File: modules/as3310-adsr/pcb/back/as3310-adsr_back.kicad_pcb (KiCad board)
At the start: 2 copper layers, 18.3 x 94 mm, 23 parts, among them J1 IDC Header 2x8, J2 Pin Socket 1x9, U1 AS3310, U2 TL071

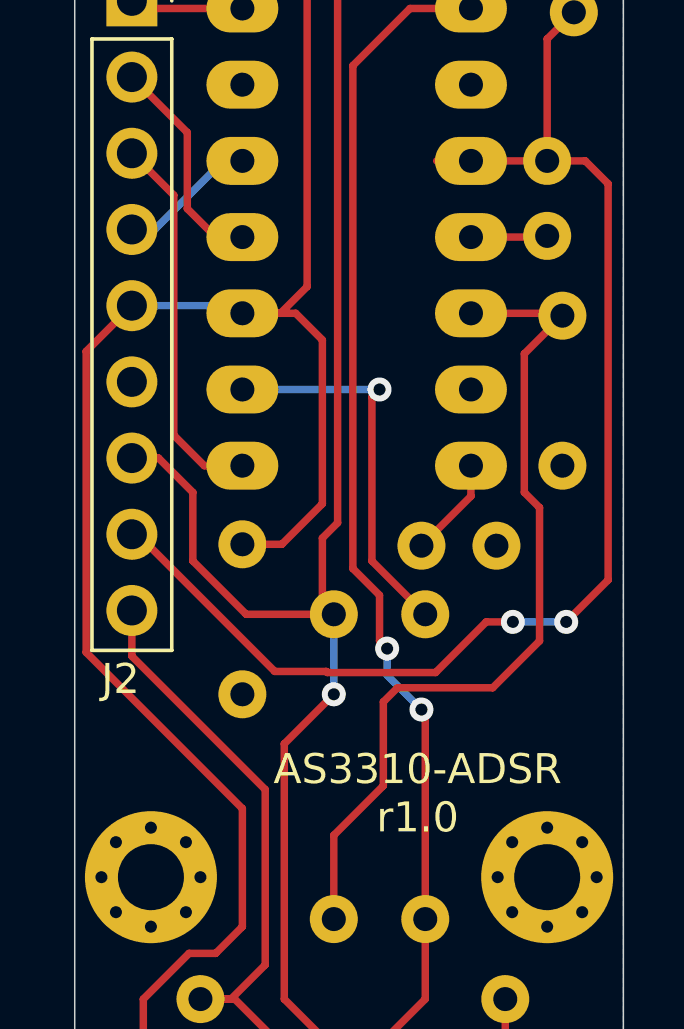
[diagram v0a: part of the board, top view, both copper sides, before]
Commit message: modules: as3310-adsr: new revision for back pcb: 1.1
the module was missing a diode in the gate input to avoid burning the
AS3310 by applying negative voltage.

I fixed my boards by cutting and scrapping the gate track, close to R3
top pin and soldering an SMD version of 1N4148, like this:

https://filebin.xyz/UGnlaM44cwMN2fDaeGj87lC2
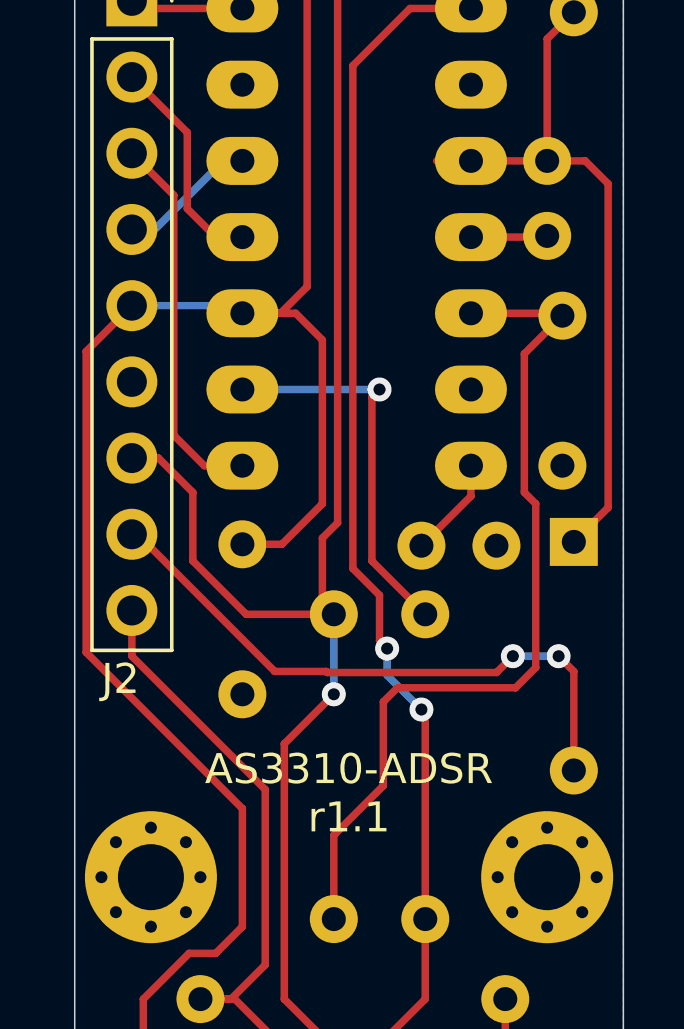
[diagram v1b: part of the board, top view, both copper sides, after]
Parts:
- added D1: 1N4148, Diode_THT:D_DO-35_SOD27_P7.62mm_Horizontal, B.Cu at (163.3, 114.0)
- C2: value 3n -> 3.3n
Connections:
- C2 pad 1: GATE -> Net-(C2-Pad1)
- R1 pad 2: GATE -> Net-(C2-Pad1)
- U1 pad 4: GATE -> Net-(C2-Pad1)
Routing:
- net Net-(C2-Pad1): track 0.00 -> 23.8 mm
- net GATE: track 43.6 -> 20.4 mm
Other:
- board text added: "AS3310-ADSR r1.1"
- board text removed: "AS3310-ADSR r1.0"

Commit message: modules: as3310-adsr: back: upgrade to kicad 6
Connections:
- J1 pad 11: (no net) -> unconnected-(J1-Pad11)
- J1 pad 12: (no net) -> unconnected-(J1-Pad12)
- J1 pad 13: (no net) -> unconnected-(J1-Pad13)
- J1 pad 14: (no net) -> unconnected-(J1-Pad14)
- J1 pad 15: (no net) -> unconnected-(J1-Pad15)
- J1 pad 16: (no net) -> unconnected-(J1-Pad16)
- U1 pad 16: (no net) -> unconnected-(U1-Pad16)
- U1 pad 3: (no net) -> unconnected-(U1-Pad3)
- U2 pad 1: (no net) -> unconnected-(U2-Pad1)
- U2 pad 5: (no net) -> unconnected-(U2-Pad5)
- U2 pad 8: (no net) -> unconnected-(U2-Pad8)
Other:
- net class Default removed

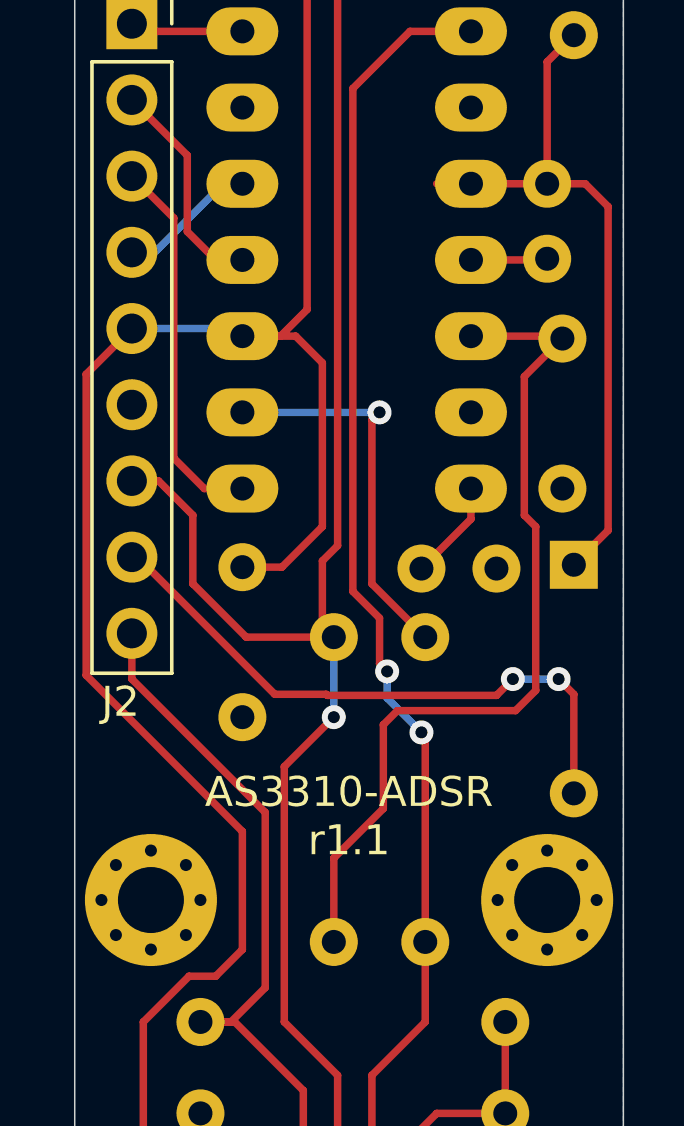
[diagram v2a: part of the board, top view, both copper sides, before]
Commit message: modules: as3310-adsr: back: remove unconnected nets
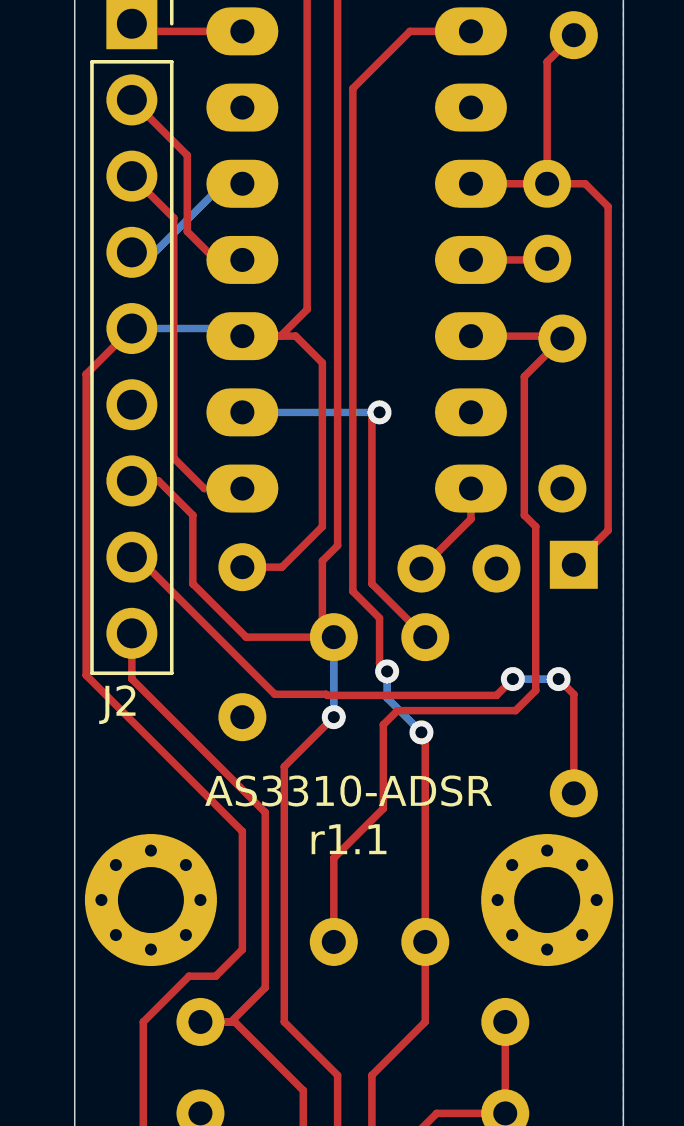
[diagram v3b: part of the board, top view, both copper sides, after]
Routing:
- net Net-(C2-Pad1): track 23.8 -> 22.6 mm
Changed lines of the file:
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@@
   (segment (start 158.369 129.286) (end 156.591 131.064) (width 0.25) (layer "F.Cu") (net 11))
   (segment (start 159.893 96.266) (end 157.861 96.266) (width 0.25) (layer "F.Cu") (net 11))
-  (segment (start 158.115 126.365) (end 158.369 126.619) (width 0.25) (layer "F.Cu") (net 11))
   (via (at 157.099 117.602) (size 0.8) (drill 0.4) (layers "F.Cu" "B.Cu") (net 11))
   (via (at 158.242 119.634) (size 0.8) (drill 0.4) (layers "F.Cu" "B.Cu") (net 11))
@@
   (segment (start 153.416 140.589) (end 154.305 139.7) (width 0.25) (layer "F.Cu") (net 14))
   (segment (start 153.035 122.301) (end 148.59 117.856) (width 0.25) (layer "F.Cu") (net 14))
-  (segment (start 156.845 108.966) (end 156.845 108.966) (width 0.25) (layer "F.Cu") (net 15))
   (segment (start 156.591 109.22) (end 156.845 108.966) (width 0.25) (layer "F.Cu") (net 15))
   (segment (start 156.591 114.681) (end 156.591 109.22) (width 0.25) (layer "F.Cu") (net 15))
@@
   (segment (start 164.465 102.108) (end 163.703 101.346) (width 0.25) (layer "F.Cu") (net 17))
   (segment (start 162.433 97.282) (end 163.322 96.393) (width 0.25) (layer "F.Cu") (net 17))
-  (segment (start 158.75 101.346) (end 159.893 101.346) (width 0.25) (layer "F.Cu") (net 17))
   (zone (net 1) (net_name "GND") (layer "B.Cu") (hatch edge 0.508)
     (connect_pads (clearance 0.508))

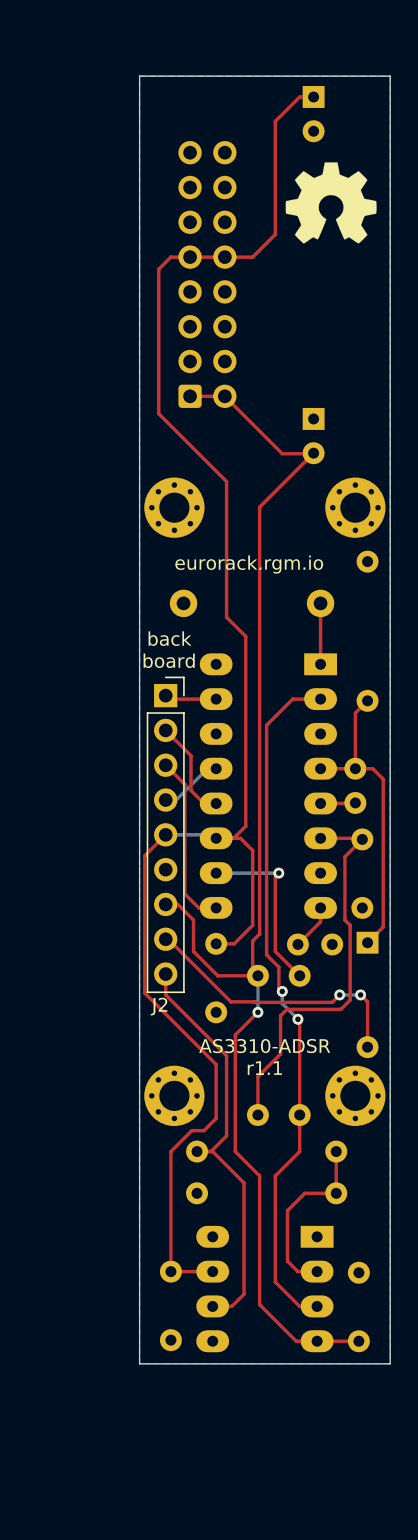
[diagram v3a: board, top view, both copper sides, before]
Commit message: modules: as3310-adsr: back: revision A (redesign)
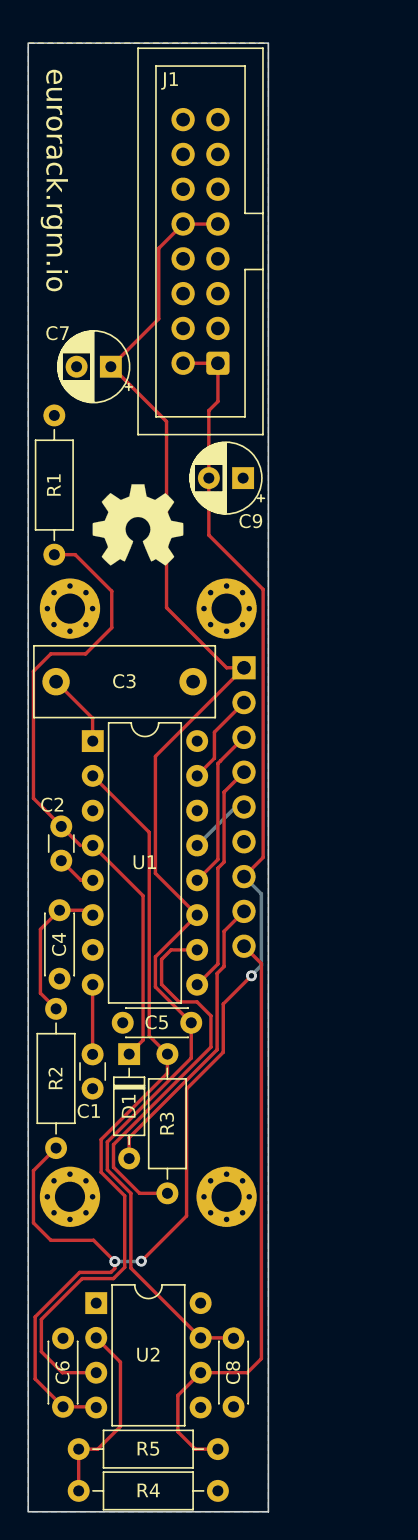
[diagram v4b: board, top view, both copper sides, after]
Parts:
- added REF**: Eurorack_PCB_4HP, eurorack:Eurorack_PCB_4HP, F.Cu at (147.3, 102.0)
- C1, C2, C3, C7, C9, D1, R1, R2, R3, R4, R5: moved to F.Cu
- C4, C5, C6, C8: footprint Capacitor_THT:C_Disc_D4.7mm_W2.5mm_P5.00mm -> Capacitor_THT:C_Disc_D4.3mm_W1.9mm_P5.00mm; moved to F.Cu
- J1: value IDC Header 2x8 -> Eurorack PSU; footprint Connector_IDC:IDC-Header_2x08_P2.54mm_Vertical -> eurorack:IDC-Header_2x08_P2.54mm_Vertical; moved to F.Cu
- J2: moved to B.Cu
- U1: footprint Package_DIP:DIP-16_W7.62mm_LongPads -> Package_DIP:DIP-16_W7.62mm; moved to F.Cu
- U2: footprint Package_DIP:DIP-8_W7.62mm_LongPads -> Package_DIP:DIP-8_W7.62mm; moved to F.Cu
- moved H3 54.4 mm to (141.6, 132.6)
- moved H2 35.8 mm to (153.0, 89.7)
- moved R4 28.7 mm to (142.2, 154.1), turned to 0 degrees
- moved REF** 27.4 mm to (146.6, 83.6)
- moved R1 25.2 mm to (140.5, 75.6)
- moved C7 24.6 mm to (144.6, 72.0), turned to 180 degrees
- moved C4 22.7 mm to (140.8, 116.7)
- moved C6 22.1 mm to (141.1, 147.9)
- moved C2 21.9 mm to (141.0, 105.6)
- moved R5 21.8 mm to (152.4, 151.0), turned to 180 degrees
- moved C3 20.1 mm to (140.6, 95.0), turned to 0 degrees
- moved D1 19.2 mm to (145.9, 122.2)
- moved R3 18.6 mm to (148.7, 132.3), turned to 90 degrees
- moved U1 17.5 mm to (143.3, 99.3), turned to 0 degrees
- moved C1 17.0 mm to (143.3, 122.2), turned to -90 degrees
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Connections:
- H1 pad 1: (no net) -> GND
- H2 pad 1: (no net) -> GND
- H3 pad 1: (no net) -> GND
- H4 pad 1: (no net) -> GND
- J2 pad 1: ATTACK -> +12V
- J2 pad 2: DECAY -> ATTACK
- J2 pad 3: SUSTAIN -> DECAY
- J2 pad 4: RELEASE -> SUSTAIN
- J2 pad 5: +12V -> RELEASE
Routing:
- net Net-(C2-Pad1): track 22.6 -> 46.3 mm
- net Net-(C4-Pad2): track 29.0 -> 10.8 mm
- net +12V: track 122.3 -> 104.9 mm
- net Net-(R3-Pad1): track 12.9 -> 28.0 mm, vias 1 -> 0
- net -12V: track 94.9 -> 107.6 mm, vias 1 -> 3
- net OUT: track 31.4 -> 43.9 mm
- net ENVOUT: track 50.9 -> 55.5 mm, vias 2 -> 0
- net DECAY: track 7.38 -> 11.8 mm
- net SUSTAIN: track 12.7 -> 16.9 mm
- net ATTACK: track 3.79 -> 6.77 mm
- net Net-(C1-Pad1): track 3.35 -> 5.09 mm
- net GATE: track 20.4 -> 21.5 mm, vias 2 -> 0
- net Net-(C3-Pad1): track 4.44 -> 5.44 mm
- net Net-(R4-Pad1): track 13.3 -> 14.0 mm
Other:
- board size 18.3 x 94 mm -> 17.5 x 107.2 mm
- board text added: "as3310 adsr Rev. A"
- board text added: "back"
- board text removed: "AS3310-ADSR r1.1"
- board text removed: "back board"
